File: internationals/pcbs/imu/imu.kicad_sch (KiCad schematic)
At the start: 17 parts, among them J1 5V-JST-XH-B2B, J2 5V-JST-XH-B2B, J3 5V-JST-XH-B2B, J4 IMU-JST-XH-B4B, J5 BT-UART-JST-XH-B4B, J6 Top-UART-JST-XH-B2B, J7 Breakout-Header-01x04, J8 Breakout-Header-01x04, J9 Breakout-Header-01x02, SW1 SW_Push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

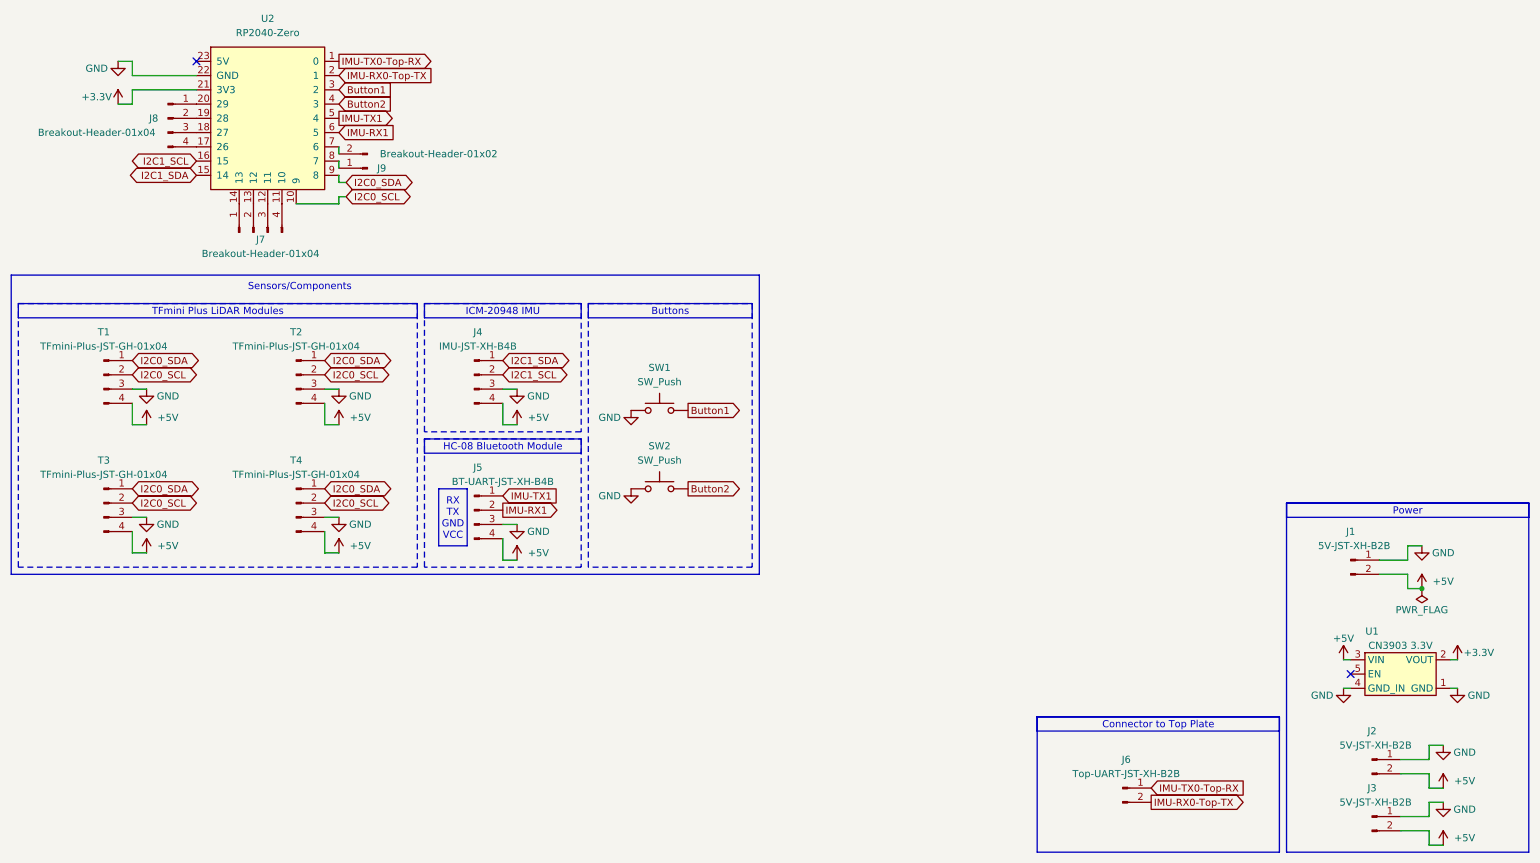
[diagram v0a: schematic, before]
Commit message: pcbs: imu: feat: add I2C pull-ups and IMU voltage selector
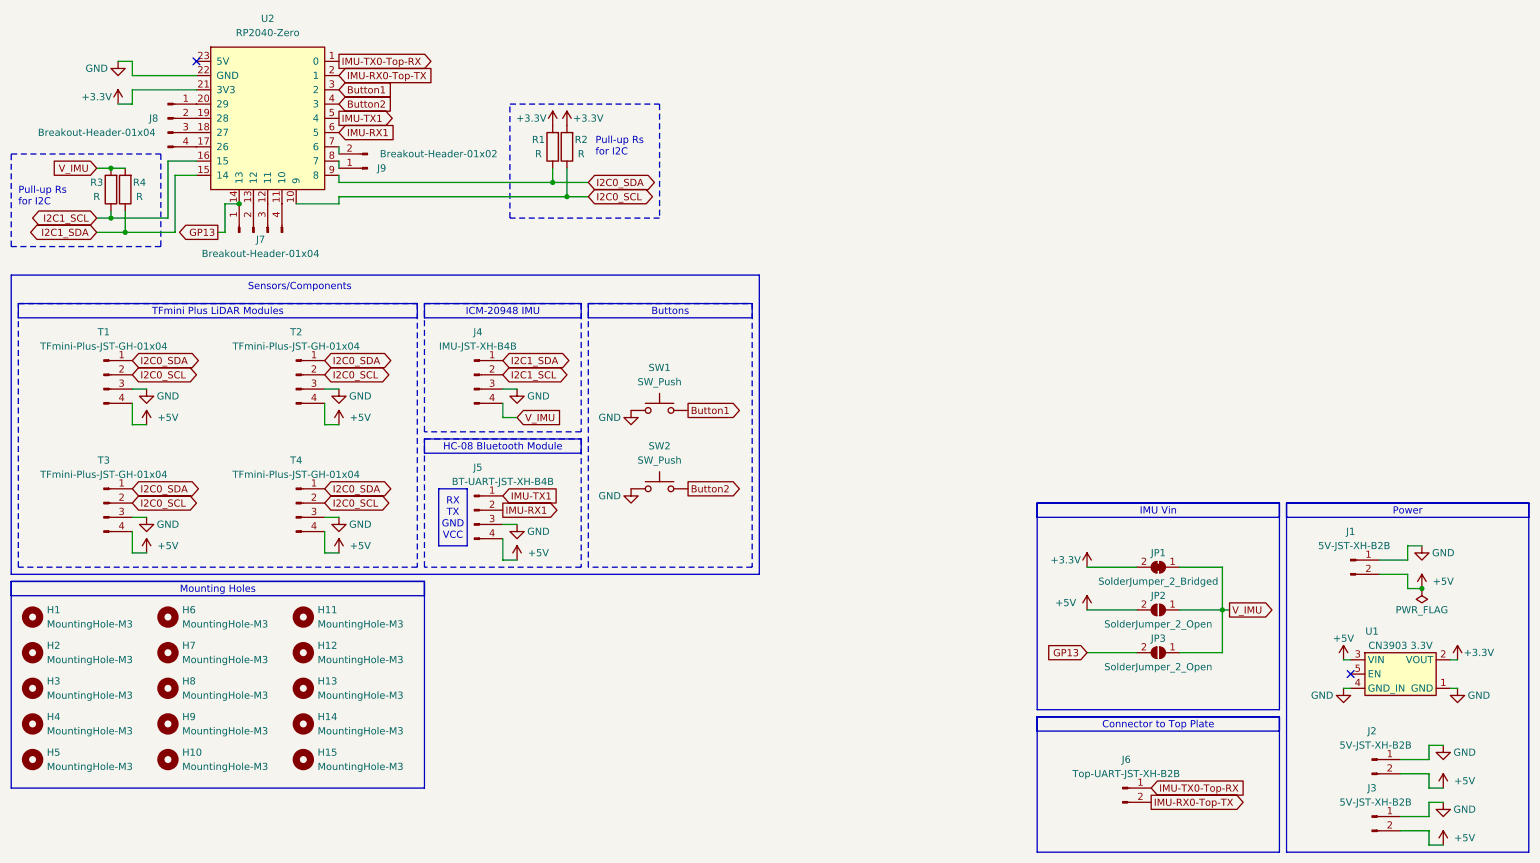
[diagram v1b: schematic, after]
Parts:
- added H1, H10, H11, H12, H13, H14, H15, H2, H3, H4, H5, H6, H7, H8, H9: MountingHole-M3, MountingHole:MountingHole_3.2mm_M3_Pad_Via, symbol Mechanical:MountingHole
- added JP1: SolderJumper_2_Bridged, Jumper:SolderJumper-2_P1.3mm_Bridged_RoundedPad1.0x1.5mm, symbol Jumper:SolderJumper_2_Bridged
- added JP2, JP3: SolderJumper_2_Open, Jumper:SolderJumper-2_P1.3mm_Open_RoundedPad1.0x1.5mm, symbol Jumper:SolderJumper_2_Open
- added R1, R2, R3, R4: R, PCM_Resistor_THT_AKL:R_Axial_DIN0204_L3.6mm_D1.6mm_P5.08mm_Horizontal, symbol Device:R
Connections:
- net +3.3V: now also JP1.2 (B), R1.2, R2.2
- net +5V: now also JP2.2 (B); no longer J4.4 (Pin_4)
- net I2C0_SCL: now also R2.1
- net I2C0_SDA: now also R1.1
- net I2C1_SCL: now also R3.1
- net I2C1_SDA: now also R4.1
- net GP13: now reaches J7.1 (Pin_1), U2.14 (13)
- net GP13: now also JP3.2 (B)
- new net V_IMU: J4.4 (Pin_4), JP1.1 (A), JP2.1 (A), JP3.1 (A), R3.2, R4.2
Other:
- note added: "Pull-up Rs for I2C"
